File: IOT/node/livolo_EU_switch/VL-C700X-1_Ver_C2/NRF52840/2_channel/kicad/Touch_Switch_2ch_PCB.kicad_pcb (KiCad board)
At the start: 2 copper layers, 43.4 x 43.2 mm, 57 parts, among them CN1 2X7P, U1 NRF52840-QIAA-R, U2 TS1, U3 Antenna 2.4GHz, U5 TMP112, U6 CY8C4014LQI-421T, U7 TS1, X1 32MHz, X2 32.768KHz, X3 ICSP

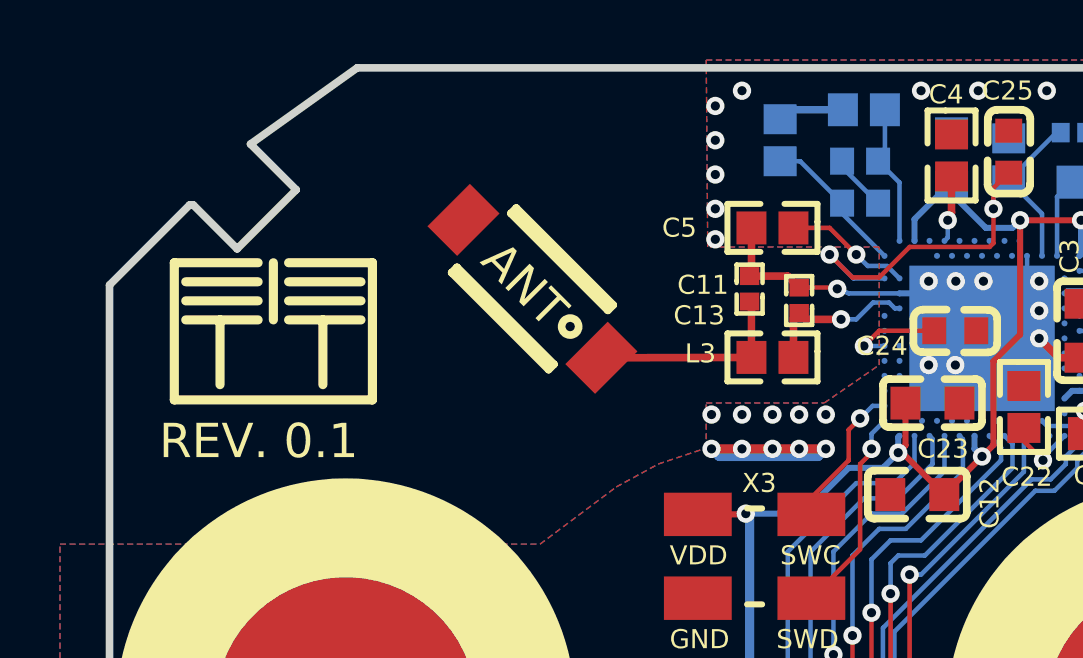
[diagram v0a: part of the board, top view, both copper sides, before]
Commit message: fixed the NRF52840 footprint for touch switches
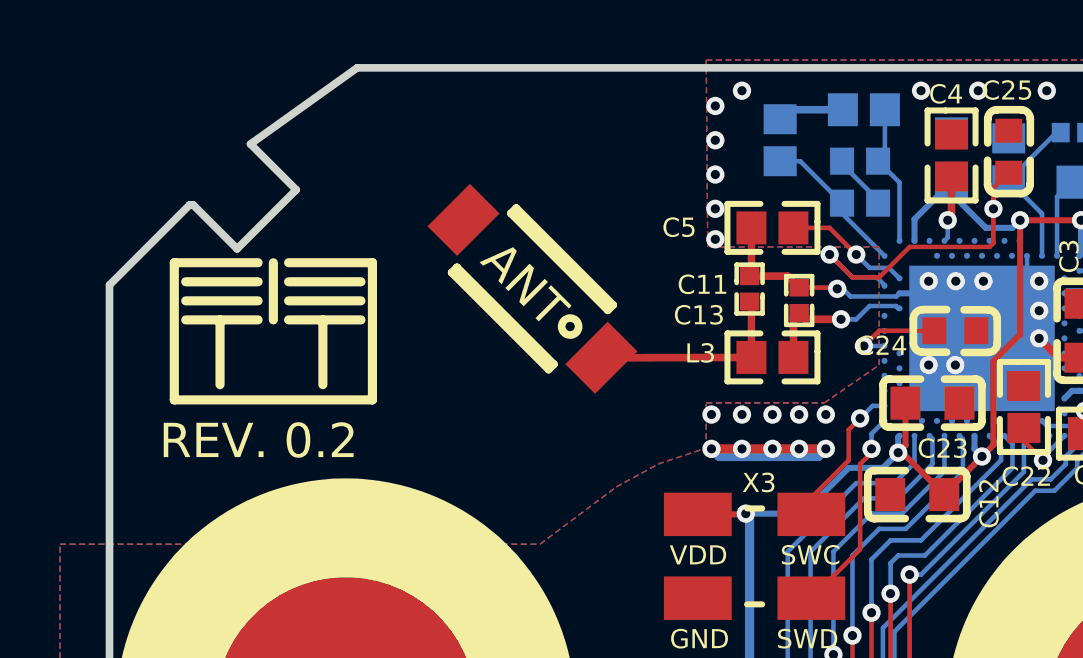
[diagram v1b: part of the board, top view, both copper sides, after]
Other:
- net class Default: clearance 0.2 -> 0.15; trace_width 0.25 -> 0.15
- rule trace_clearance: 0.2 -> 0.15
- rule trace_min: 0.2 -> 0.15
- board text added: "REV. 0.2"
- board text removed: "REV. 0.1"
